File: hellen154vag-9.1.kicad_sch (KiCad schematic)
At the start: 63 parts, among them J1 USB_B_Mini, M1 Module-can-0.1, M2 Module-power5-0.1, M3 Module-mcu-0.1, M4 Module-input-0.1, M5 Module-knock-0.1, M6 Module-output-0.1, M7 Module-ign8-0.1, M8 Module-power12-0.1, P1 368255-2

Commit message: Added 33816 sub schematic changed 121 connector to 154 connector Initial draft schematic. Many nets are not properly connected.
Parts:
- added P? (x2): rusEFI_Lib:284617-1, MODULE, symbol 284617-1:284617-1
- P1: footprint hellen121vag:368255-2 -> rusEFI_Lib:284617-1
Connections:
- net at P1.23: no longer R3.1
- now unconnected: P1.21, R2.1, R8.1
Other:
- added sheet Common_Rail_MC33816 (Common_Rail_MC33816.kicad_sch)
- moved on the sheet: C1, D1, F1, F2, J1, M1, M2, M3A, M3B, M3C, M3D, M4A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

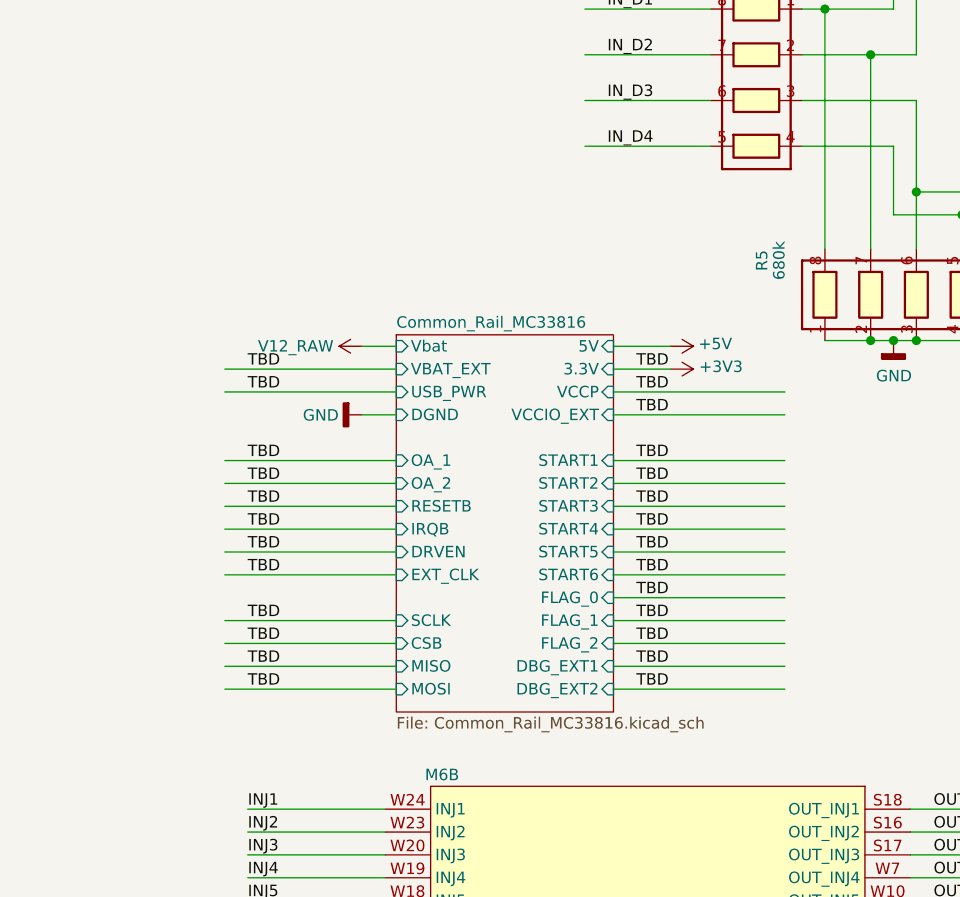
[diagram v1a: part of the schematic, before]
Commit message: Added injector net names to the sheet labels.
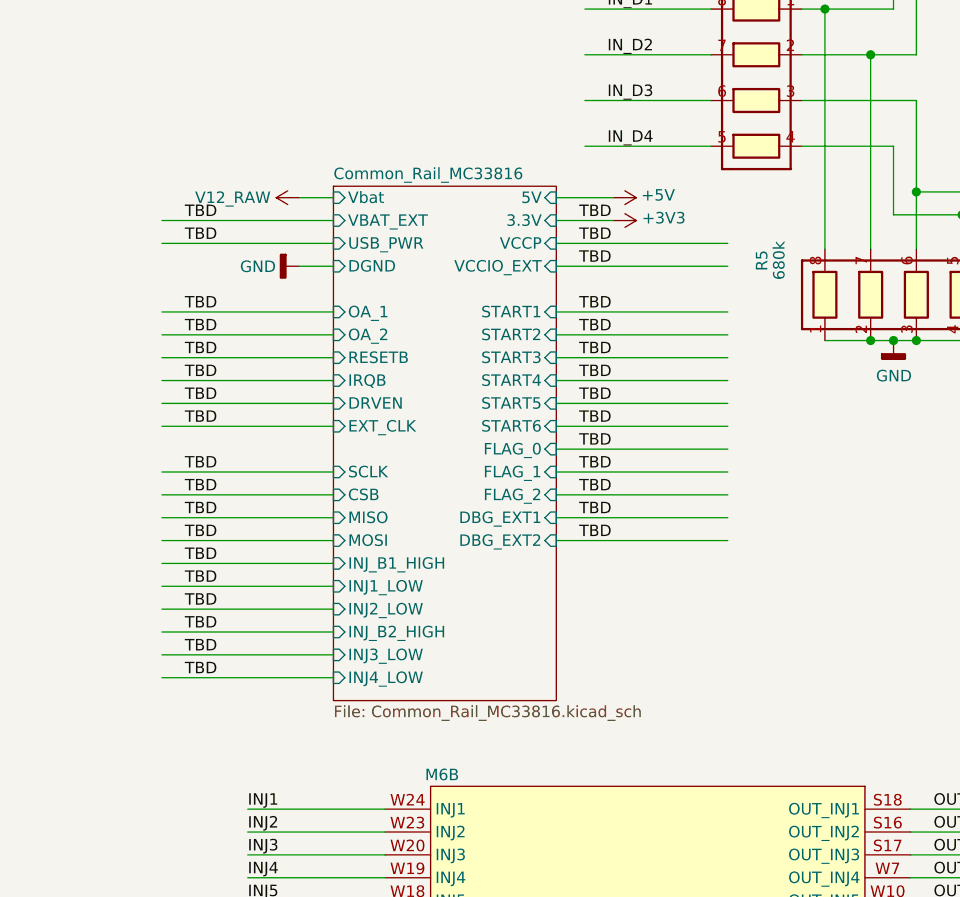
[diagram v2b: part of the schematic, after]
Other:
- sheet Common_Rail_MC33816 ports: added INJ1_LOW, INJ2_LOW, INJ3_LOW, INJ4_LOW, INJ_B1_HIGH, INJ_B2_HIGH; removed none

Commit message: Initial attempt at connecting connector to circuits. Currently many errors.
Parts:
- added W1, W2, W? (x152): TEST, rusEFI_Lib:SM0805_jumper, symbol hellen-one-common:TEST
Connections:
- net +12V: now also W?.2, W?.2, W?.2, W?.2, W?.2
- net CANH: now also W?.2; no longer P1.60
- net CANL: now also W?.2; no longer P1.58
- net GND: now also W?.2, W?.2, W?.2, W?.2, W?.2, W?.2, W?.2, W?.2, W?.2, W?.2
- net IN_CAM1: now also W?.2; no longer P1.86
- net IN_CLT: now also W?.2; no longer P1.93
- net IN_IAT: now also W?.2; no longer P1.26
- net IN_MAF: now also W?.2; no longer P1.29
- net IN_MAP2: now also W?.2; no longer P1.101
- net IN_TPS1: now also W?.2; no longer P1.92
- net IN_TPS2: now also W?.2; no longer P1.84
- net OUT_IGN1: now also W?.2; no longer P1.102
- net OUT_IGN2: now also W?.2; no longer P1.7
- net OUT_IGN3: now also W?.2; no longer P1.111
- net OUT_IGN4: now also W?.2; no longer P1.94
- net OUT_WASTEGATE: now also W?.2; no longer P1.104
- net V5A: now also W?.2, W?.2, W?.2, W?.2, W?.2, W?.2; no longer P1.72
- net VREF1: no longer P1.90
- net at P?.100 (40): now also W?.1
- net at P?.101 (41): now also W?.1
- net at P?.102 (42): now also W?.1
- net at P?.103 (43): now also W?.1
- net at P?.104 (44): now also W?.1
- net at P?.105 (45): now also W?.1
- net at P?.106 (46): now also W?.1
- net at P?.107 (47): now also W?.1
- net at P?.108 (48): now also W?.1
- net at P?.109 (49): now also W?.1
- net at P?.110 (50): now also W?.1
- net at P?.111 (51): now also W?.1
- net at P?.112 (52): now also W?.1
- net at P?.113 (53): now also W?.1
- net at P?.114 (54): now also W?.1
- net at P?.115 (55): now also W?.1
- net at P?.116 (56): now also W?.1
- net at P?.117 (57): now also W?.1
- net at P?.118 (58): now also W?.1
- net at P?.119 (59): now also W?.1
- net at P?.120 (60): now also W?.1
- net at P?.121 (61): now also W?.1
- net at P?.122 (62): now also W?.1
- net at P?.123 (63): now also W?.1
- net at P?.124 (64): now also W?.1
- net at P?.125 (65): now also W?.1
- net at P?.126 (66): now also W?.1
- net at P?.127 (67): now also W?.1
- net at P?.128 (68): now also W?.1
- net at P?.129 (69): now also W?.1
- net at P?.130 (70): now also W?.1
- net at P?.131 (71): now also W?.1
- net at P?.132 (72): now also W?.1
- net at P?.133 (73): now also W?.1
- net at P?.134 (74): now also W?.1
- net at P?.135 (75): now also W?.1
- net at P?.136 (76): now also W?.1
- net at P?.137 (77): now also W?.1
- net at P?.138 (78): now also W?.1
- net at P?.139 (79): now also W?.1
- net at P?.140 (80): now also W?.1
- net at P?.141 (81): now also W?.1
- net at P?.142 (82): now also W?.1
- net at P?.143 (83): now also W?.1
- net at P?.144 (84): now also W?.1
- net at P?.145 (85): now also W?.1
- net at P?.146 (86): now also W?.1
- net at P?.147 (87): now also W?.1
- net at P?.148 (88): now also W?.1
- net at P?.149 (89): now also W?.1
- net at P?.150 (90): now also W?.1
- net at P?.151 (91): now also W?.1
- net at P?.152 (92): now also W?.1
- net at P?.153 (93): now also W?.1
- net at P?.154 (94): now also W?.1
- net at P?.61 (1): now also W?.1
- net at P?.62 (2): now also W?.1
- net at P?.63 (3): now also W?.1
- net at P?.64 (4): now also W?.1
- net at P?.65 (5): now also W?.1
- net at P?.66 (6): now also W?.1
- net at P?.67 (7): now also W?.1
- net at P?.68 (8): now also W?.1
- net at P?.69 (9): now also W?.1
- net at P?.70 (10): now also W?.1
- net at P?.71 (11): now also W?.1
- net at P?.72 (12): now also W?.1
- net at P?.73 (13): now also W?.1
- net at P?.74 (14): now also W?.1
- net at P?.75 (15): now also W?.1
- net at P?.76 (16): now also W?.1
- net at P?.77 (17): now also W?.1
- net at P?.78 (18): now also W?.1
- net at P?.79 (19): now also W?.1
- net at P?.80 (20): now also W?.1
- net at P?.81 (21): now also W?.1
- net at P?.82 (22): now also W?.1
- net at P?.83 (23): now also W?.1
- net at P?.84 (24): now also W?.1
- net at P?.85 (25): now also W?.1
- net at P?.86 (26): now also W?.1
- net at P?.87 (27): now also W?.1
- net at P?.88 (28): now also W?.1
- net at P?.89 (29): now also W?.1
- net at P?.90 (30): now also W?.1
- net at P?.91 (31): now also W?.1
- net at P?.92 (32): now also W?.1
- net at P?.93 (33): now also W?.1
- net at P?.94 (34): now also W?.1
- net at P?.95 (35): now also W?.1
- net at P?.96 (36): now also W?.1
- net at P?.97 (37): now also W?.1
- net at P?.98 (38): now also W?.1
- net at P?.99 (39): now also W?.1
- net at P?.1: now also W1.1
- net at P?.10: now also W?.1
- net at P?.11: now also W?.1
- net at P?.12: now also W?.1
- net at P?.13: now also W?.1
- net at P?.14: now also W?.1
- net at P?.15: now also W?.1
- net at P?.16: now also W?.1
- net at P?.17: now also W?.1
- net at P?.18: now also W?.1
- net at P?.19: now also W?.1
- net at P?.2: now also W?.1
- net at P?.20: now also W?.1
- net at P?.21: now also W?.1
- net at P?.22: now also W?.1
- net at P?.23: now also W?.1
- net at P?.24: now also W?.1
- net at P?.25: now also W?.1
- net at P?.26: now also W?.1
- net at P?.27: now also W?.1
- net at P?.28: now also W?.1
- net at P?.29: now also W?.1
- net at P?.3: now also W?.1
- net at P?.30: now also W?.1
- net at P?.31: now also W?.1
- net at P?.32: now also W?.1
- net at P?.33: now also W?.1
- net at P?.34: now also W?.1
- net at P?.35: now also W?.1
- net at P?.36: now also W?.1
- net at P?.37: now also W?.1
- net at P?.38: now also W?.1
- net at P?.39: now also W?.1
- net at P?.4: now also W?.1
- net at P?.40: now also W?.1
- net at P?.41: now also W?.1
- net at P?.42: now also W?.1
- net at P?.43: now also W?.1
- net at P?.44: now also W?.1
- net at P?.45: now also W?.1
- net at P?.46: now also W?.1
- net at P?.47: now also W?.1
- net at P?.48: now also W?.1
- net at P?.49: now also W?.1
- net at P?.5: now also W2.1
- net at P?.50: now also W?.1
- net at P?.51: now also W?.1
- net at P?.52: now also W?.1
- net at P?.53: now also W?.1
- net at P?.54: now also W?.1
- net at P?.55: now also W?.1
- net at P?.56: now also W?.1
- net at P?.57: now also W?.1
- net at P?.58: now also W?.1
- net at P?.59: now also W?.1
- net at P?.6: now also W?.1
- net at P?.60: now also W?.1
- net at P?.7: now also W?.1
- net at P?.8: now also W?.1
- net at P?.9: now also W?.1
- new net INJ_B1_1LOW: W?.2
- new net INJ_B1_2LOW: W1.2
- new net INJ_B1_HIGH: W?.2, W?.2
- new net INJ_B2_3LOW: W?.2
- new net INJ_B2_4LOW: W?.2
- new net INJ_B2_HIGH: W?.2, W?.2
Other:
- moved on the sheet: R2, R3, R8

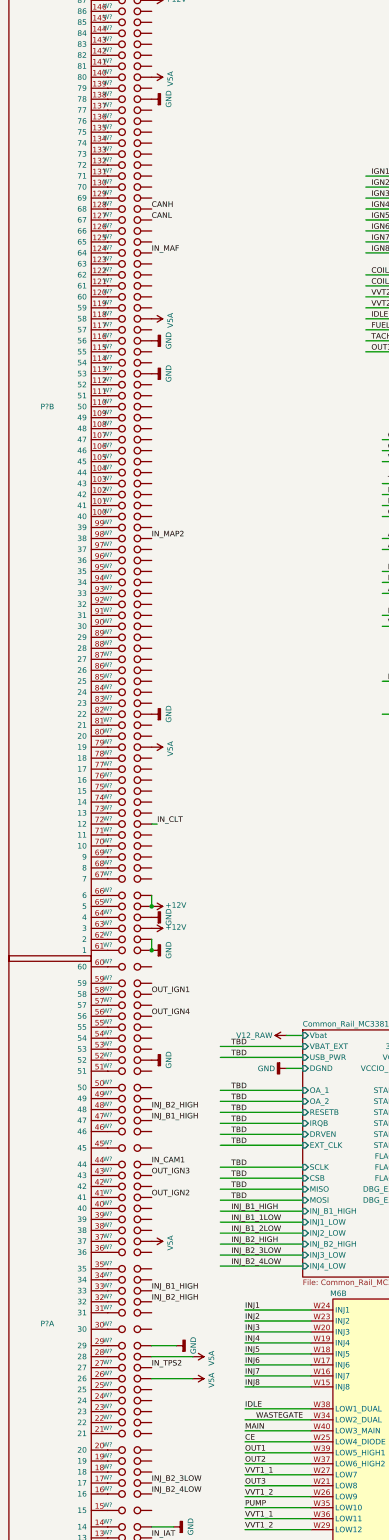
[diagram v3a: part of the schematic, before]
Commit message: Connected several more nets. Still missing ETB, and VR. It still needs several nets to be connected.
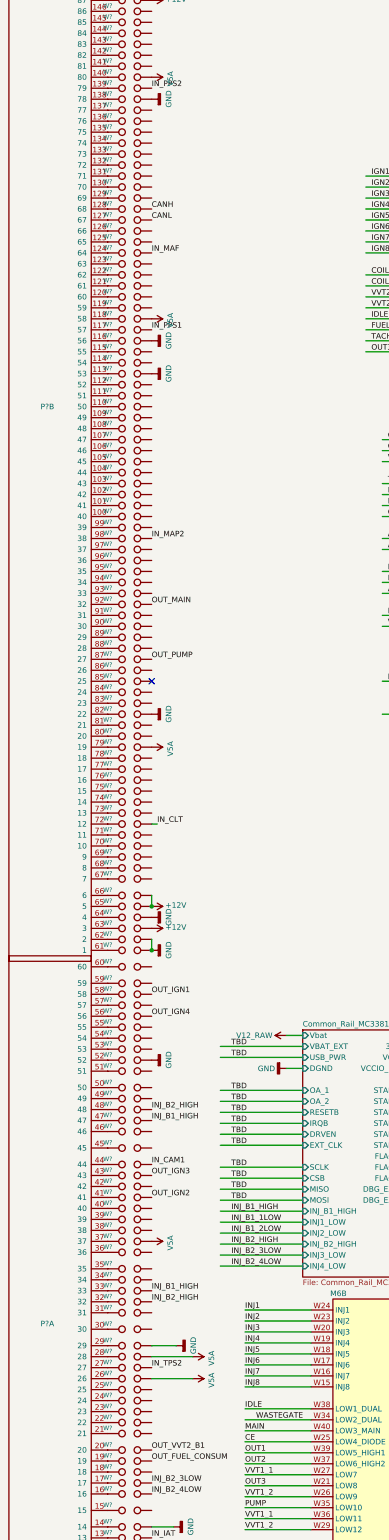
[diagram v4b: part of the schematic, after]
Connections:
- net IN_PPS1: now also W?.2
- net IN_PPS2: now also W?.2
- net OUT_FUEL_CONSUM: now also W?.2
- net OUT_MAIN: now also W?.2
- net OUT_PUMP: now also W?.2
- net OUT_VVT2_B1: now also W?.2
- no-connect marks 71 -> 72
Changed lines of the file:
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@@
   (no_connect (at -33.02 361.95))
   (no_connect (at -33.02 369.57))
+  (no_connect (at 43.18 189.23))
   (no_connect (at 106.68 18.415))
   (no_connect (at 106.68 20.955))
@@
     (effects (font (size 1.27 1.27)) (justify left bottom))
   )
+  (label "IN_PPS2" (at 43.18 52.07 0)
+    (effects (font (size 1.27 1.27)) (justify left bottom))
+  )
   (label "CANH" (at 43.18 80.01 0)
     (effects (font (size 1.27 1.27)) (justify left bottom))
@@
     (effects (font (size 1.27 1.27)) (justify left bottom))
   )
+  (label "IN_PPS1" (at 43.18 107.95 0)
+    (effects (font (size 1.27 1.27)) (justify left bottom))
+  )
   (label "IN_MAP2" (at 43.18 156.21 0)
     (effects (font (size 1.27 1.27)) (justify left bottom))
   )
+  (label "OUT_MAIN" (at 43.18 171.45 0)
+    (effects (font (size 1.27 1.27)) (justify left bottom))
+  )
+  (label "OUT_PUMP" (at 43.18 184.15 0)
+    (effects (font (size 1.27 1.27)) (justify left bottom))
+  )
   (label "OUT_IGN1" (at 43.18 261.62 0)
     (effects (font (size 1.27 1.27)) (justify left bottom))
@@
     (effects (font (size 1.27 1.27)) (justify left bottom))
   )
+  (label "OUT_VVT2_B1" (at 43.18 367.03 0)
+    (effects (font (size 1.27 1.27)) (justify left bottom))
+  )
+  (label "OUT_FUEL_CONSUM" (at 43.18 369.57 0)
+    (effects (font (size 1.27 1.27)) (justify left bottom))
+  )
